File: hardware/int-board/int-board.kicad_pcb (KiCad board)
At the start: 2 copper layers, 59 x 85 mm, 35 parts, among them J1 PTSM 0,5/4-HH-2,5-THR, J2 PTSM 0,5/4-HH-2,5-THR, J3 PTSM 0,5/4-HH-2,5-THR, J4 PTSM 0,5/4-HH-2,5-THR, J5 Pi 40-pin socket, J6 PTSM 0,5/5-HH-2,5-THR, J7 PTSM 0,5/4-HH-2,5-THR, J8 SP-C SP-E COM, J9 GPIO breakout, U1 LTV-847, U2 LTV-847, U3 LTV-847

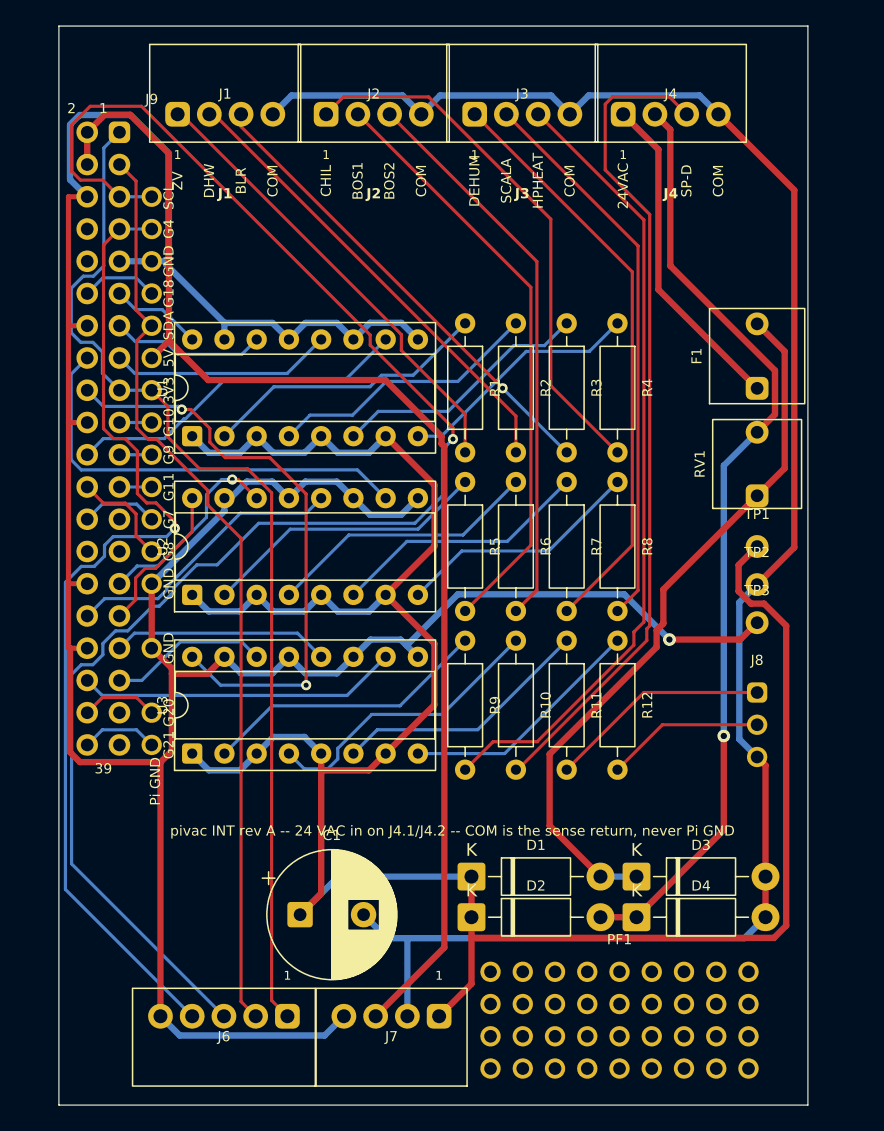
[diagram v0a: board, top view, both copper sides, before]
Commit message: hardware: INT link headers move into the housing's right-hand slot; review checklist in docs
The enclosure leaves no clearance around the board except the opening for
the four top-edge plugs and a slot on the right-hand side, rows 9-23, the
height of a PTSM socket (David, 2026-09-12). J6 and J7 sit in that slot
with their entries facing the edge, pin row 6.3 mm inside it so the pads
clear the rib's bulges at x 49.8; the MOV position, test points and J8
move to the bottom-left field the links vacated. Header pin 1 stays open
on the board like the spare grounds: the column blocks a track from pin 1
to pin 17, and the router otherwise reached the link from pin 1 and left
17's breakout stranded. A via keepout ring 0.8 mm inside the outline stops
the router placing vias against the 0.3 mm edge rule, which the DSN does
not carry. gen-boards.py also gains the GND_BUS_X import it lost when the
constants moved to gen_tables.py.

Routed, DRC clean, schematic parity kept; Gerbers re-exported. The
"before you order" checklist is docs/rpi-io-boards-review.md.

Co-Authored-By: Claude Fable 5.1 <noreply@anthropic.com>
Claude-Session: https://claude.ai/code/session_01WPMStupqhasFMcGr3goMno
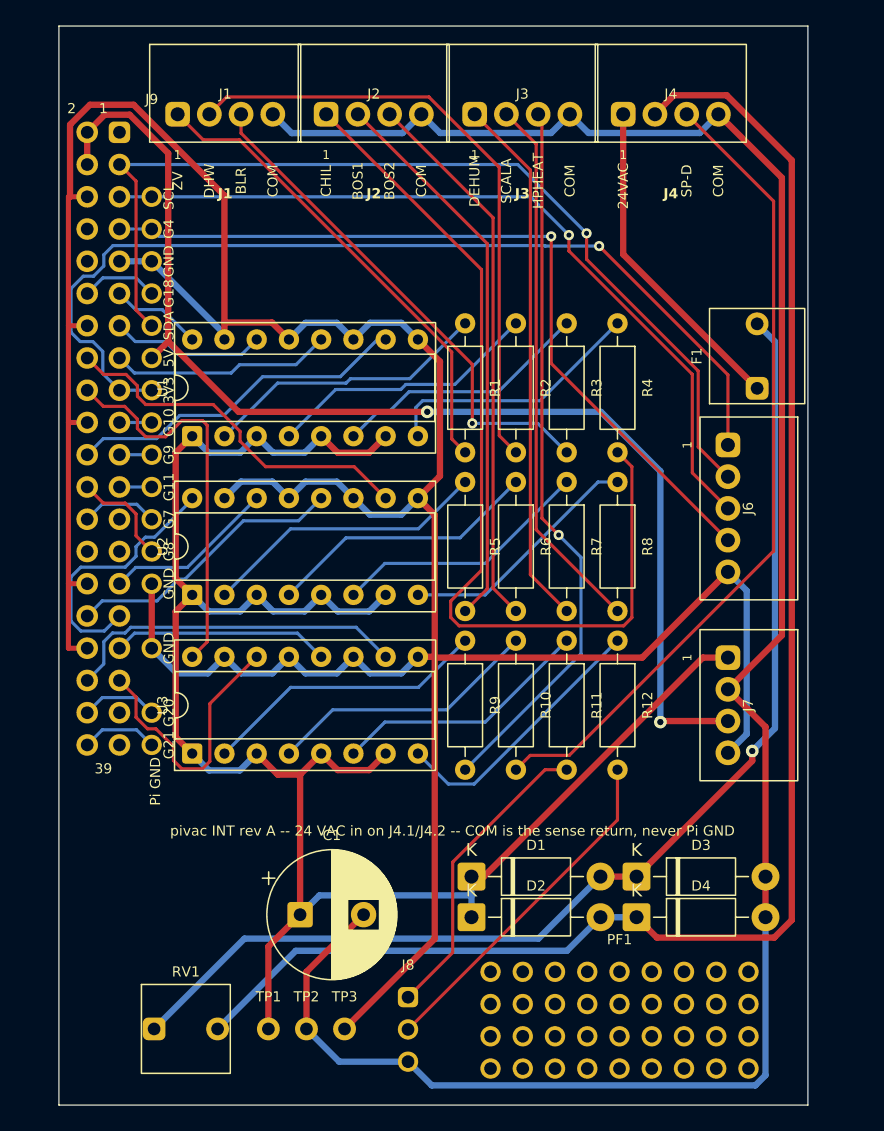
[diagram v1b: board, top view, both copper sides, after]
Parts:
- moved RV1 63.3 mm to (10.0, 79.0), turned to 0 degrees
- moved J6 56.4 mm to (52.7, 38.0), turned to -90 degrees
- moved TP1 54.1 mm to (16.5, 79.0)
- moved TP2 49.9 mm to (19.5, 79.0)
- moved TP3 45.6 mm to (22.5, 79.0)
- moved J8 36.5 mm to (27.5, 76.5)
- moved J7 36.1 mm to (52.7, 53.5), turned to -90 degrees
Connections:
- J5 pad 1: 3V3 -> (no net)
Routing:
- net SCL: track 125.7 -> 63.4 mm
- net ACC: track 74.5 -> 123.5 mm, vias 1 -> 0
- net VS: track 184.3 -> 148.6 mm
- net ACF: track 56.6 -> 91.6 mm, vias 0 -> 1
- net S_CHIL: track 42.8 -> 74.0 mm
- net COM: track 146.4 -> 168.7 mm
- net GPIO24: track 46.2 -> 30.8 mm, vias 2 -> 0
- net GPIO4: track 79.1 -> 63.9 mm
- net S_SP-E: track 12.5 -> 27.3 mm
- net S_DHW: track 36.9 -> 48.7 mm
- net GND: track 245.4 -> 255.8 mm, vias 1 -> 0
- net GPIO19: track 12.6 -> 21.6 mm
- net GPIO6: track 12.1 -> 20.7 mm
- net 3V3: track 83.0 -> 76.1 mm, vias 0 -> 1
- net S_SP-C: track 17.5 -> 24.1 mm
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
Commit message: hardware: every INT component-side part held to the DIP-socket height; the Pi mapped under the board
The cover's inner depth is unmeasured, but the built board proves it clears
a DIP socket with its chip, about 8 mm, so no fitted part may stand taller.
The 12.5 mm radial capacitor becomes a 100 uF 63 V axial lying flat along
the bottom-left field (6.5 x 18, 6.9 mm); 100 uF holds the 35 V rail's
ripple to 2.8 V at 34 mA and the value is not critical. The PTC disc and the
MOV position lie flat on new pivac footprints. The test points, spare pads
and proto field move to suit.

Appendix A.3 of the plan maps the Pi 4B's connectors onto the INT board
from the RP-008343 mechanical drawing, with the room each leaves on the
solder side at the 16 mm socket stack: none under the USB stacks, where
every joint is trimmed flush, as the built board already requires.

Routed, DRC clean, schematic parity kept; Gerbers re-exported.

Co-Authored-By: Claude Fable 5.1 <noreply@anthropic.com>
Claude-Session: https://claude.ai/code/session_01WPMStupqhasFMcGr3goMno
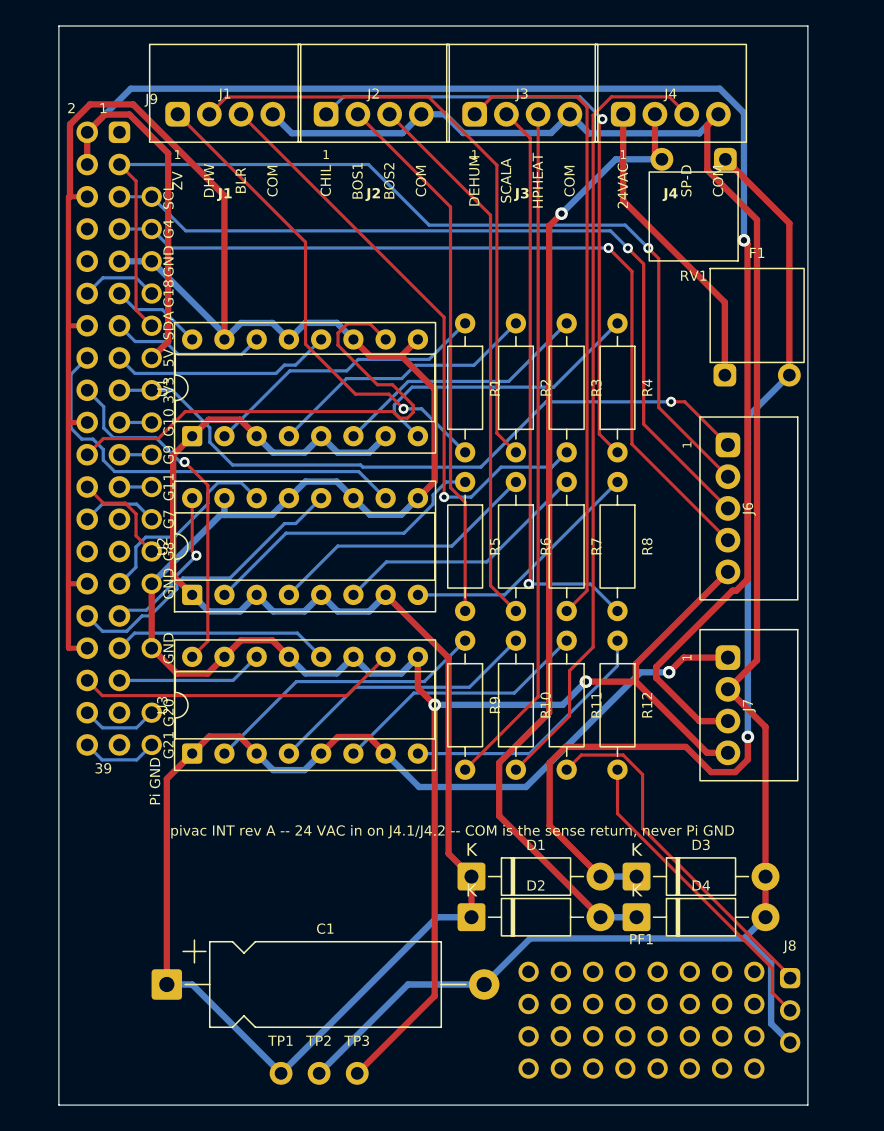
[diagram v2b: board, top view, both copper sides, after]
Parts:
- C1: value 220u 50V -> 100u 63V axial; footprint CP_Radial_D10.0mm_P5.00mm -> CP_Axial_L18.0mm_D6.5mm_P25.00mm_Horizontal
- F1: value PTC 0.1A -> PTC 0.1A 60V; footprint pivac:PTC_Radial_P5.08 -> pivac:PTC_Radial_P5.08_Flat
- PF1: footprint pivac:Proto_9x4 -> pivac:Proto_8x4
- RV1: footprint pivac:MOV_Radial_P5.0 -> pivac:MOV_Radial_P5.0_Flat
- moved RV1 79.3 mm to (50.0, 10.5), turned to 180 degrees
- moved J8 30.1 mm to (57.6, 75.0)
- moved C1 11.9 mm to (8.50, 75.5)
- moved TP1 3.64 mm to (17.5, 82.5)
- moved TP2 3.64 mm to (20.5, 82.5)
- moved TP3 3.64 mm to (23.5, 82.5)
- moved PF1 3.00 mm to (37.0, 74.5)
- moved F1 1.50 mm to (55.0, 27.5), turned to 0 degrees
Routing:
- net ACC: track 123.5 -> 77.1 mm, vias 0 -> 1
- net +5V: track 95.5 -> 136.2 mm, vias 2 -> 1
- net VS: track 148.6 -> 180.7 mm, vias 0 -> 1
- net S_CHIL: track 74.0 -> 50.0 mm, vias 0 -> 1
- net 3V3: track 76.1 -> 54.7 mm
- net GPIO25: track 27.3 -> 41.4 mm
- net COM: track 168.7 -> 156.2 mm
- net ACF: track 91.6 -> 81.6 mm
- net GPIO19: track 21.6 -> 11.6 mm
- net S_DEHUM: track 42.1 -> 50.1 mm
- net GPIO6: track 20.7 -> 12.9 mm, vias 0 -> 1
- net S_BLR: track 40.3 -> 47.9 mm
- net GND: track 255.8 -> 249.7 mm, vias 0 -> 2
- net GPIO23: track 29.0 -> 33.6 mm
- net S_SP-C: track 24.1 -> 27.9 mm
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
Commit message: hardware: no through-hole part over the Pi's USB stacks; the capacitor stands between J4 and J6
The USB shells are Pi ground and the rectifier's nets are 35 V above COM,
so a pin tail under a USB stack, where the 16 mm socket stack leaves no
room, is a short waiting to happen (David, 2026-09-12). The bottom-left
field now carries nothing: the capacitor stands between J4 and the link
slot, right of the resistor columns (pitch 3.3 mm) and left of the housing
rib, with the PTC and the MOV position lying flat beside it; the four
diodes form one column at the bottom right past the USB stacks, with the
test points and the spare-channel pads (now a row) below them; the
prototyping field is gone. The link headers' pin row moves to 6.0 mm inside
the edge so their courtyards clear the capacitor's.

docs/rpi-io-boards-review.md and the review page gain a table of what
every reference designator on each board is for.

Routed, DRC clean, schematic parity kept; Gerbers re-exported.

Co-Authored-By: Claude Fable 5.1 <noreply@anthropic.com>
Claude-Session: https://claude.ai/code/session_01WPMStupqhasFMcGr3goMno
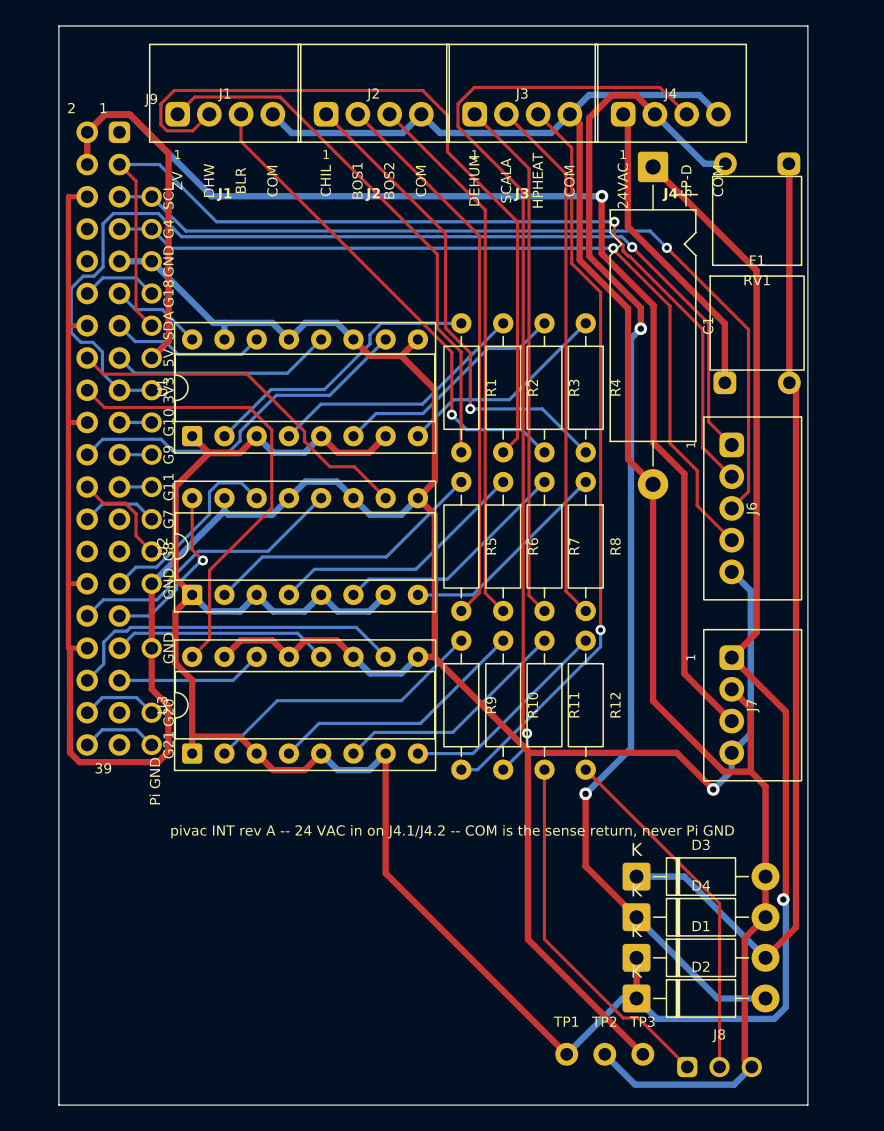
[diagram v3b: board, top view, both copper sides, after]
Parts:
- removed PF1: proto, pivac:Proto_8x4
- J8: footprint pivac:Pads_1x3 -> pivac:Pads_3x1
- moved C1 74.9 mm to (46.8, 11.1), turned to -90 degrees
- moved TP1 22.5 mm to (40.0, 81.0)
- moved TP2 22.5 mm to (43.0, 81.0)
- moved TP3 22.5 mm to (46.0, 81.0)
- moved D1 14.5 mm to (45.5, 73.4)
- moved D2 14.5 mm to (45.5, 76.6)
- moved J8 10.7 mm to (49.5, 82.0)
- moved RV1 5.01 mm to (55.0, 10.8)
- moved R12 2.50 mm to (41.5, 48.4)
- moved R4 2.50 mm to (41.5, 23.4)
- moved R8 2.50 mm to (41.5, 35.9)
- moved R11 1.75 mm to (38.2, 48.4)
- moved R3 1.75 mm to (38.2, 23.4)
- moved R7 1.75 mm to (38.2, 35.9)
- moved R10 1.00 mm to (35.0, 48.4)
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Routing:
- net 3V3: track 54.7 -> 81.2 mm
- net VS: track 180.7 -> 206.6 mm
- net +5V: track 136.2 -> 116.8 mm
- net ACC: track 77.1 -> 94.6 mm, vias 1 -> 2
- net COM: track 156.2 -> 142.6 mm
- net GPIO25: track 41.4 -> 28.5 mm
- net S_SP-D: track 62.6 -> 74.9 mm, vias 0 -> 1
- net S_CHIL: track 50.0 -> 38.4 mm
- net S_DHW: track 48.7 -> 59.3 mm
- net S_BLR: track 47.9 -> 39.1 mm
- net S_DEHUM: track 50.1 -> 41.4 mm
- net GPIO24: track 27.6 -> 36.3 mm, vias 1 -> 0
- net K4: track 23.5 -> 17.0 mm
- net GPIO23: track 33.6 -> 28.5 mm
- net ACF: track 81.6 -> 76.6 mm, vias 1 -> 0
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
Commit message: hardware: silkscreen tidied, MOV position dropped, copper plots for the review
Plug designators sit below their pin labels (J4's beside the capacitor),
the resistor references run along their bodies, the diode references sit
at the board edge end of each diode, the link header references sit on the
rib strip beside them, the capacitor's beside its lower pad, and the empty
bottom field says why it is empty. The MOV position is gone: the strip
beside the capacitor holds the PTC and the J4 labels, and a clamp on a
class 2 transformer's 24 VAC is a nicety. GPIO8's run from header pin 24
to its breakout pad, which threads the column twice through 0.84 mm gaps,
is laid by hand because the router managed it only sometimes. EXT: C1's
reference moves below the part, clear of the H2 label.

Both boards carry front and back copper plots (back mirrored) from
kicad-cli for checking traces; the review document shows both faces of
each board and the copper.

Co-Authored-By: Claude Fable 5.1 <noreply@anthropic.com>
Claude-Session: https://claude.ai/code/session_01WPMStupqhasFMcGr3goMno
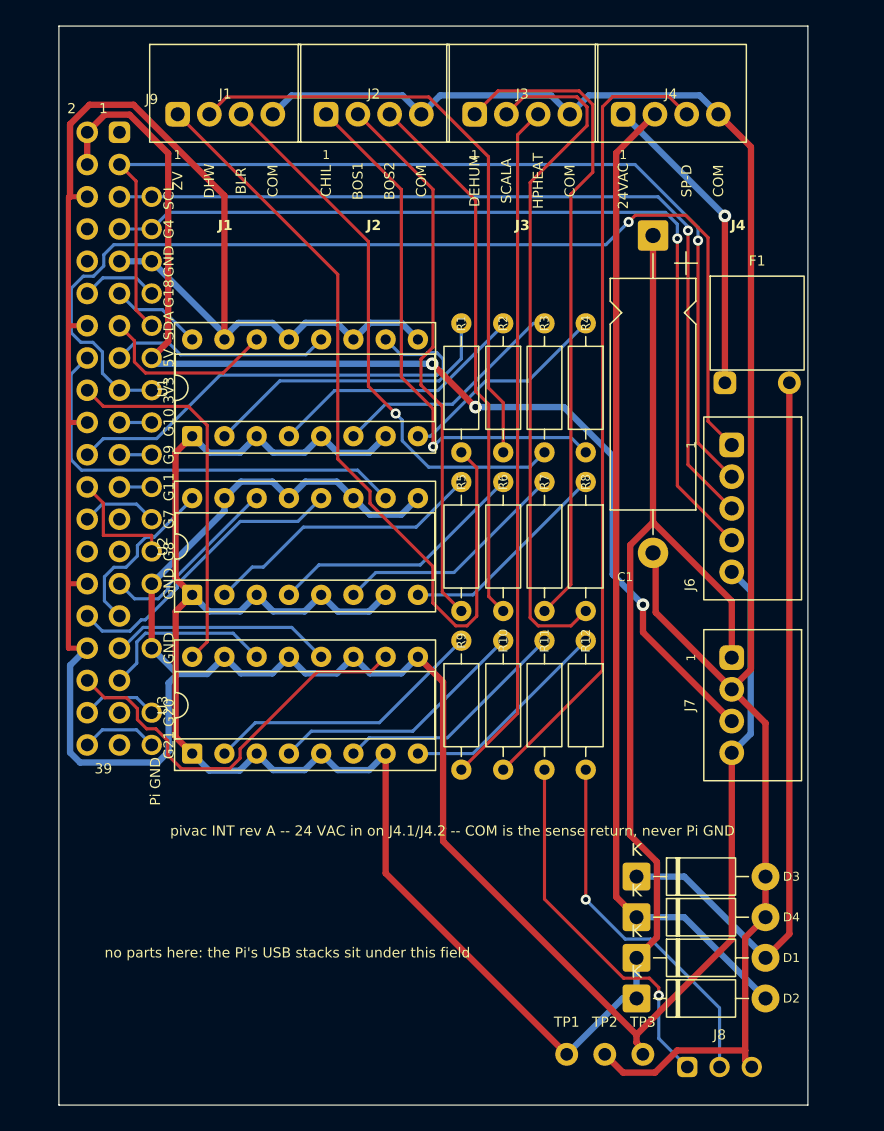
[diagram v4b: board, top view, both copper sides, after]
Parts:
- removed RV1: MOV 39V, pivac:MOV_Radial_P5.0_Flat
- moved C1 5.40 mm to (46.8, 16.5)
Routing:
- net +5V: track 116.8 -> 91.7 mm, vias 1 -> 3
- net S_ZV: track 42.5 -> 64.7 mm
- net GND: track 248.6 -> 266.5 mm, vias 1 -> 0
- net ACF: track 76.6 -> 58.9 mm
- net ACC: track 94.6 -> 78.0 mm, vias 2 -> 0
- net S_SCALA: track 41.7 -> 54.5 mm
- net S_SP-D: track 74.9 -> 63.0 mm, vias 1 -> 0
- net VS: track 206.6 -> 195.2 mm, vias 1 -> 0
- net S_DHW: track 59.3 -> 48.3 mm
- net S_DEHUM: track 41.4 -> 52.0 mm
- net GPIO25: track 28.5 -> 36.9 mm
- net GPIO24: track 36.3 -> 29.3 mm
- net GPIO23: track 28.5 -> 34.6 mm
- net GPIO4: track 66.4 -> 71.5 mm
- net S_HPHEAT: track 59.0 -> 54.1 mm, vias 1 -> 0
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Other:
- board text added: "no parts here: the Pi's USB stacks sit under this field"
